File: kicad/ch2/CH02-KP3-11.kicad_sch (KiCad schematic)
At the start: 7 parts

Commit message: regular
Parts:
- removed I6: 5, symbol Simulation_SPICE:IDC
- removed R29: 10, symbol Device:R_US
- removed R30: 3, symbol Device:R_US
- removed R31, R32: 6, symbol Device:R_US
- removed R33: 16, symbol Device:R_US
- removed V12: 30, symbol Simulation_SPICE:VDC
- added E1: ESOURCE, symbol Simulation_SPICE:ESOURCE
- added R37: 4, symbol Device:R_US
- added R38: 6, symbol Device:R_US
- added V13: 12, symbol Simulation_SPICE:VDC
- added V14: 4, symbol Simulation_SPICE:VDC
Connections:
- net 0: now also E1.4 (C-), R38.2, V14.1
- new net: R37.1, V13.1
- new net: E1.1 (N+), R37.2
- new net: E1.2 (N-), V14.2
- new net vo: E1.3 (C+), R38.1, V13.2

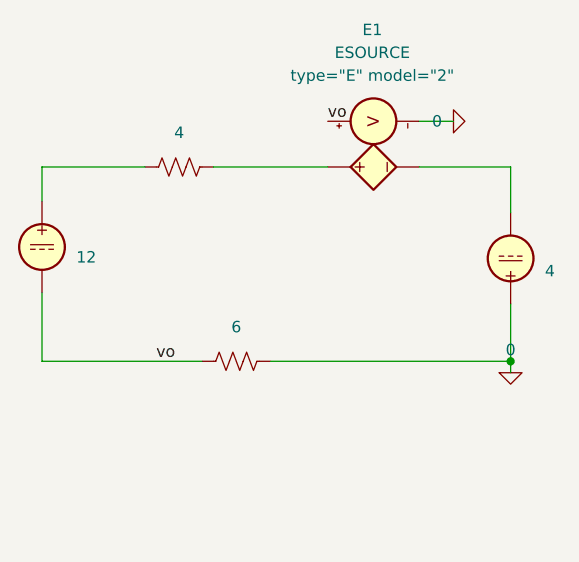
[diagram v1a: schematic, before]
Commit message: fix subsheet sim problem
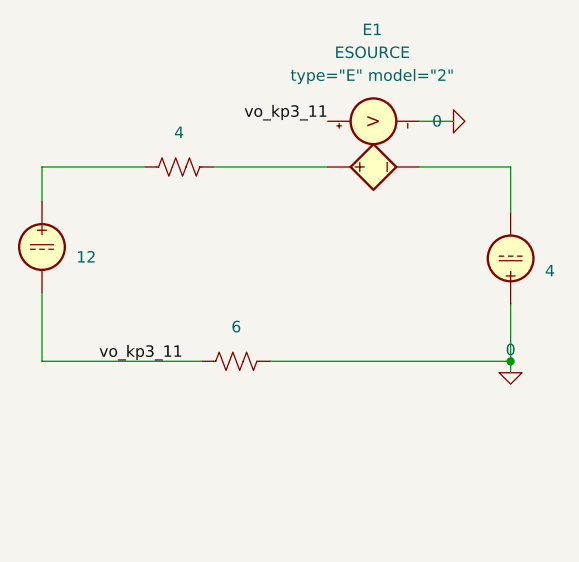
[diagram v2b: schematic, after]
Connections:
- net vo renamed vo_kp3_11
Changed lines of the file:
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@@
 		)
 	)
-	(label "vo"
-		(at 76.2 83.82 0)
+	(label "vo_kp3_11"
+		(at 69.85 83.82 0)
 		(effects
 			(font
@@
 		)
 	)
-	(label "vo"
-		(at 95.25 57.15 0)
+	(label "vo_kp3_11"
+		(at 95.25 57.15 180)
 		(effects
 			(font
 				(size 1.27 1.27)
 			)
-			(justify left bottom)
+			(justify right bottom)
 		)
 	)
